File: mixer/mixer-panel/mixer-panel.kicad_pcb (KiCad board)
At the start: 2 copper layers, 40.3 x 128.5 mm, 14 parts

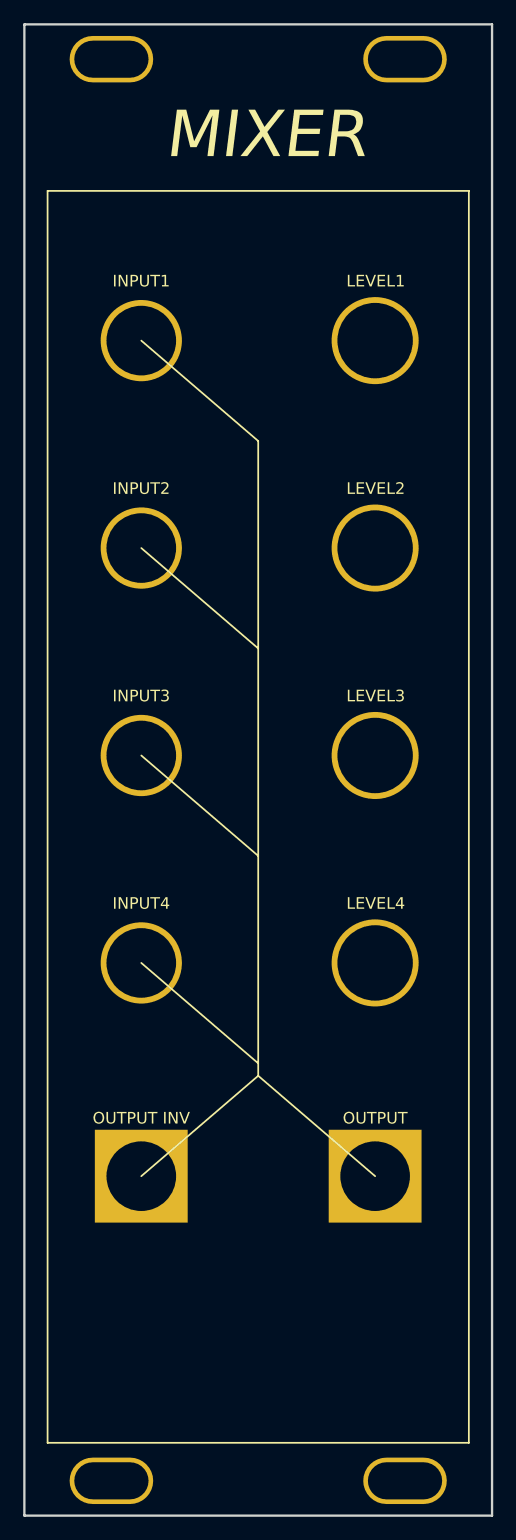
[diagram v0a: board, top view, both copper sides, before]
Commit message: Added rev2 of mixer. Fixed opamp configuation and panel connector layout
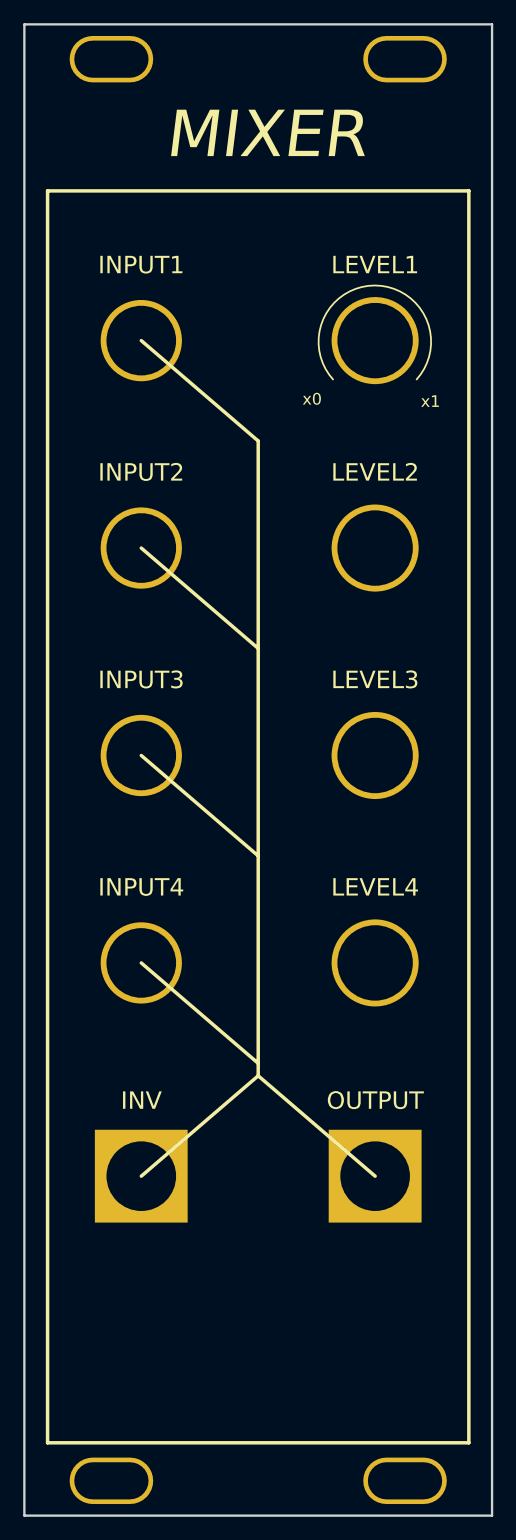
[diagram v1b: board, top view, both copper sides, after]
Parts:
- INV: renamed from OUTPUT INV
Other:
- board text added: "REV2"
- board text added: "x0"
- board text added: "x1"
- board text removed: "REV1"
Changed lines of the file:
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@@
   (footprint "Eurorack_Panel_Designs:3.5MM_Jack_Panel_Output_Plated" locked (layer "F.Cu")
     (at 147.225 132.75)
-    (fp_text reference "OUTPUT" (at 0 -5 unlocked) (layer "F.SilkS")
-      (effects (font (size 1 1) (thickness 0.15)))
+    (fp_text reference "OUTPUT" (at 0 -6.5 unlocked) (layer "F.SilkS")
+      (effects (font (size 1.5 1.5) (thickness 0.3)))
     )
     (fp_text value "3.5MM_Jack_Panel_Output_Plated" (at 0.826 -6.818 unlocked) (layer "F.Fab") hide
@@
     (at 147.225 78.625)
     (attr through_hole)
-    (fp_text reference "LEVEL2" (at 0.0508 -5.1308 unlocked) (layer "F.SilkS")
-      (effects (font (size 1 1) (thickness 0.15)))
+    (fp_text reference "LEVEL2" (at 0 -6.505 unlocked) (layer "F.SilkS")
+      (effects (font (size 1.5 1.5) (thickness 0.3)))
     )
     (fp_text value "Alpha_Plastic_Pot_Plated" (at 0 -5.4356 unlocked) (layer "F.Fab") hide
-      (effects (font (size 1 1) (thickness 0.15)))
-    )
-    (fp_text user "${REFERENCE}" (at 0 2.5 unlocked) (layer "F.Fab")
       (effects (font (size 1 1) (thickness 0.15)))
     )
@@
   (footprint "Eurorack_Panel_Designs:3.5MM_Jack_Panel_Output_Plated" (layer "F.Cu")
     (at 127.075 132.75)
-    (fp_text reference "OUTPUT INV" (at 0 -5 unlocked) (layer "F.SilkS")
-      (effects (font (size 1 1) (thickness 0.15)))
+    (fp_text reference "INV" (at 0 -6.5 unlocked) (layer "F.SilkS")
+      (effects (font (size 1.5 1.5) (thickness 0.3)))
     )
     (fp_text value "3.5MM_Jack_Panel_Output_Plated" (at 0.826 -6.818 unlocked) (layer "F.Fab") hide
@@
   (footprint "Eurorack_Panel_Designs:3.5MM_Jack_Panel_Input_Plated" (layer "F.Cu")
     (at 127.075 96.5)
-    (fp_text reference "INPUT3" (at 0 -5.1308 unlocked) (layer "F.SilkS")
-      (effects (font (size 1 1) (thickness 0.15)))
+    (fp_text reference "INPUT3" (at 0 -6.5 unlocked) (layer "F.SilkS")
+      (effects (font (size 1.5 1.5) (thickness 0.3)))
     )
     (fp_text value "3.5MM_Jack_Panel_Input_Plated" (at 0 -4.1896 unlocked) (layer "F.Fab") hide
@@
     (at 147.225 96.5)
     (attr through_hole)
-    (fp_text reference "LEVEL3" (at 0.0508 -5.1308 unlocked) (layer "F.SilkS")
-      (effects (font (size 1 1) (thickness 0.15)))
+    (fp_text reference "LEVEL3" (at 0 -6.5 unlocked) (layer "F.SilkS")
+      (effects (font (size 1.5 1.5) (thickness 0.3)))
     )
     (fp_text value "Alpha_Plastic_Pot_Plated" (at 0 -5.4356 unlocked) (layer "F.Fab") hide
@@
   (footprint "Eurorack_Panel_Designs:3.5MM_Jack_Panel_Input_Plated" (layer "F.Cu")
     (at 127.075 60.75)
-    (fp_text reference "INPUT1" (at 0 -5.1308 unlocked) (layer "F.SilkS")
-      (effects (font (size 1 1) (thickness 0.15)))
+    (fp_text reference "INPUT1" (at 0 -6.5 unlocked) (layer "F.SilkS")
+      (effects (font (size 1.5 1.5) (thickness 0.3)))
     )
     (fp_text value "3.5MM_Jack_Panel_Input_Plated" (at 0 -4.1896 unlocked) (layer "F.Fab") hide
@@
   (footprint "Eurorack_Panel_Designs:3.5MM_Jack_Panel_Input_Plated" (layer "F.Cu")
     (at 127.075 78.625)
-    (fp_text reference "INPUT2" (at 0 -5.1308 unlocked) (layer "F.SilkS")
-      (effects (font (size 1 1) (thickness 0.15)))
+    (fp_text reference "INPUT2" (at 0 -6.505 unlocked) (layer "F.SilkS")
+      (effects (font (size 1.5 1.5) (thickness 0.3)))
     )
     (fp_text value "3.5MM_Jack_Panel_Input_Plated" (at 0 -4.1896 unlocked) (layer "F.Fab") hide
@@
   (footprint "Eurorack_Panel_Designs:3.5MM_Jack_Panel_Input_Plated" (layer "F.Cu")
     (at 127.075 114.375)
-    (fp_text reference "INPUT4" (at 0 -5.1308 unlocked) (layer "F.SilkS")
-      (effects (font (size 1 1) (thickness 0.15)))
+    (fp_text reference "INPUT4" (at 0 -6.5 unlocked) (layer "F.SilkS")
+      (effects (font (size 1.5 1.5) (thickness 0.3)))
     )
     (fp_text value "3.5MM_Jack_Panel_Input_Plated" (at 0 -4.1896 unlocked) (layer "F.Fab") hide
@@
     (at 147.225 114.375)
     (attr through_hole)
-    (fp_text reference "LEVEL4" (at 0.0508 -5.1308 unlocked) (layer "F.SilkS")
-      (effects (font (size 1 1) (thickness 0.15)))
+    (fp_text reference "LEVEL4" (at 0 -6.5 unlocked) (layer "F.SilkS")
+      (effects (font (size 1.5 1.5) (thickness 0.3)))
     )
     (fp_text value "Alpha_Plastic_Pot_Plated" (at 0 -5.4356 unlocked) (layer "F.Fab") hide
@@
     (at 147.225 60.75)
     (attr through_hole)
-    (fp_text reference "LEVEL1" (at 0.0508 -5.1308 unlocked) (layer "F.SilkS")
-      (effects (font (size 1 1) (thickness 0.15)))
+    (fp_text reference "LEVEL1" (at 0 -6.5 unlocked) (layer "F.SilkS")
+      (effects (font (size 1.5 1.5) (thickness 0.3)))
     )
     (fp_text value "Alpha_Plastic_Pot_Plated" (at 0 -5.4356 unlocked) (layer "F.Fab") hide
-      (effects (font (size 1 1) (thickness 0.15)))
-    )
-    (fp_text user "${REFERENCE}" (at 0 2.5 unlocked) (layer "F.Fab")
       (effects (font (size 1 1) (thickness 0.15)))
     )
@@
     (pad "" thru_hole oval locked (at 0 0) (size 7.2 4) (drill oval 6.4 3.2) (layers *.Cu *.Mask))
   )
-  (gr_line (start 127.075 96.5) (end 137.15 105.15) (layer "F.SilkS") (width 0.15))
-  (gr_line (start 137.15 124.1) (end 147.225 132.75) (layer "F.SilkS") (width 0.15))
-  (gr_rect locked (start 119 47.85) (end 155.3 155.725) (layer "F.SilkS") (width 0.15) (fill none))
-  (gr_line (start 127.075 114.375) (end 137.15 123.025) (layer "F.SilkS") (width 0.15))
-  (gr_line (start 127.075 78.625) (end 137.15 87.275) (layer "F.SilkS") (width 0.15))
-  (gr_line (start 137.15 124.1) (end 127.075 132.75) (layer "F.SilkS") (width 0.15))
-  (gr_line (start 127.075 60.75) (end 137.15 69.4) (layer "F.SilkS") (width 0.15))
-  (gr_line (start 137.15 69.4) (end 137.15 124.1) (layer "F.SilkS") (width 0.15))
+  (gr_line (start 127.075 96.5) (end 137.15 105.15) (layer "F.SilkS") (width 0.3))
+  (gr_line (start 137.15 124.1) (end 147.225 132.75) (layer "F.SilkS") (width 0.3))
+  (gr_rect locked (start 119 47.85) (end 155.3 155.725) (layer "F.SilkS") (width 0.3) (fill none))
+  (gr_line (start 127.075 114.375) (end 137.15 123.025) (layer "F.SilkS") (width 0.3))
+  (gr_line (start 127.075 78.625) (end 137.15 87.275) (layer "F.SilkS") (width 0.3))
+  (gr_arc (start 143.6 64.098193) (mid 147.2 56) (end 150.8 64.098193) (layer "F.SilkS") (width 0.15))
+  (gr_line (start 137.15 124.1) (end 127.075 132.75) (layer "F.SilkS") (width 0.3))
+  (gr_line (start 127.075 60.75) (end 137.15 69.4) (layer "F.SilkS") (width 0.3))
+  (gr_line (start 137.15 69.4) (end 137.15 124.1) (layer "F.SilkS") (width 0.3))
   (gr_line (start 117 47.75) (end 157.3 47.75) (layer "Dwgs.User") (width 0.15))
   (gr_line (start 117 147.75) (end 157.3 147.75) (layer "Dwgs.User") (width 0.15))
   (gr_rect locked (start 117 33.5) (end 157.3 162) (layer "Edge.Cuts") (width 0.2) (fill none))
-  (gr_text "REV1" (at 137.1 158.7) (layer "B.SilkS")
+  (gr_text "REV2" (at 137.1 158.7) (layer "B.SilkS")
     (effects (font (size 1 1) (thickness 0.15)) (justify mirror))
   )
+  (gr_text "x0" (at 141.8 65.8) (layer "F.SilkS")
+    (effects (font (size 1 1) (thickness 0.15)))
+  )
+  (gr_text "x1" (at 152 66) (layer "F.SilkS")
+    (effects (font (size 1 1) (thickness 0.15)))
+  )
   (gr_text "MIXER" (at 137.8 43) (layer "F.SilkS")
-    (effects (font (size 4 4) (thickness 0.3) italic))
+    (effects (font (size 4 4) (thickness 0.35) italic))
   )
   (gr_text "PCB_BOTTOM" (at 122.4 149) (layer "Dwgs.User")

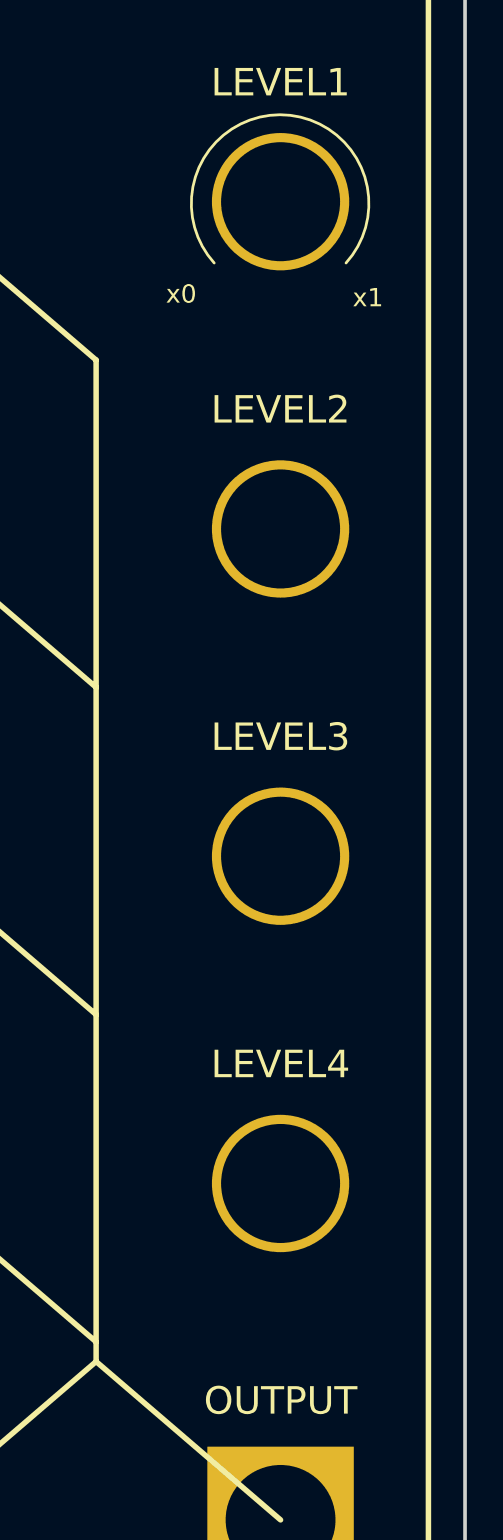
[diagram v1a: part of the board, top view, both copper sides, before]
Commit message: Updated graphics on rev2 mixer panel
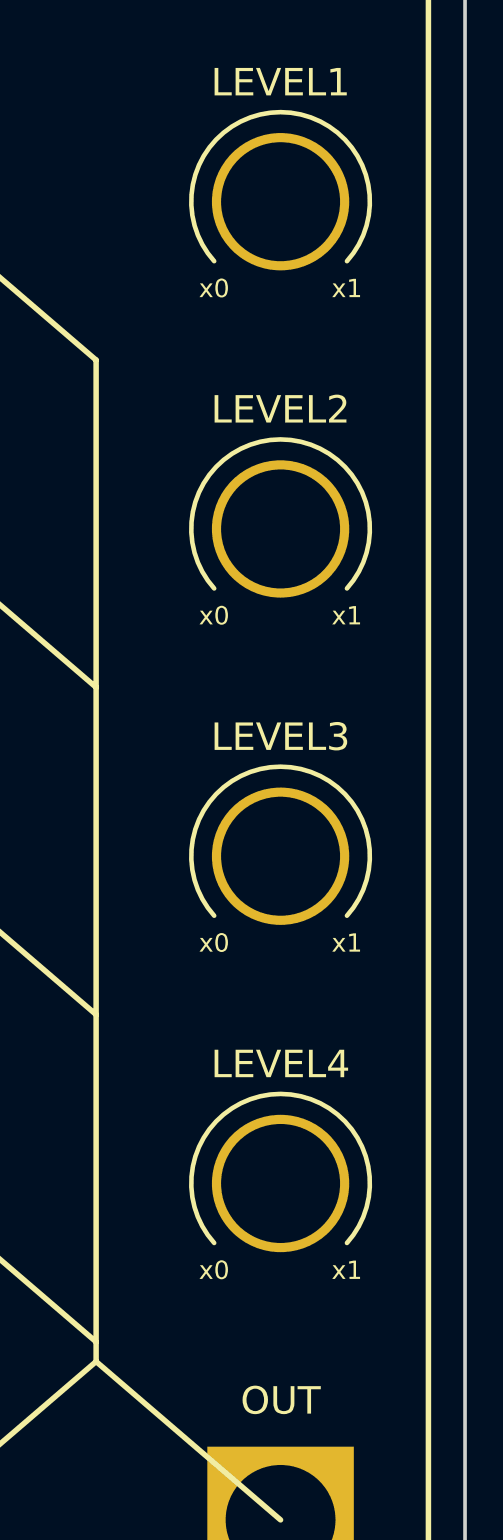
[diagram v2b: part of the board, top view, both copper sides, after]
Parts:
- renumbered OUTPUT to OUT
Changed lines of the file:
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@@
   (footprint "Eurorack_Panel_Designs:3.5MM_Jack_Panel_Output_Plated" locked (layer "F.Cu")
     (at 147.225 132.75)
-    (fp_text reference "OUTPUT" (at 0 -6.5 unlocked) (layer "F.SilkS")
+    (fp_text reference "OUT" (at 0 -6.5 unlocked) (layer "F.SilkS")
       (effects (font (size 1.5 1.5) (thickness 0.3)))
     )
@@
       (effects (font (size 1 1) (thickness 0.15)))
     )
-    (fp_text user "${REFERENCE}" (at 0 2.5 unlocked) (layer "F.Fab")
-      (effects (font (size 1 1) (thickness 0.15)))
-    )
     (pad "" thru_hole circle locked (at 0 0) (size 7.5 7.5) (drill 6.5) (layers *.Cu *.Mask))
   )
@@
     )
     (fp_text value "Alpha_Plastic_Pot_Plated" (at 0 -5.4356 unlocked) (layer "F.Fab") hide
-      (effects (font (size 1 1) (thickness 0.15)))
-    )
-    (fp_text user "${REFERENCE}" (at 0 2.5 unlocked) (layer "F.Fab")
       (effects (font (size 1 1) (thickness 0.15)))
     )
@@
   (gr_line (start 127.075 114.375) (end 137.15 123.025) (layer "F.SilkS") (width 0.3))
   (gr_line (start 127.075 78.625) (end 137.15 87.275) (layer "F.SilkS") (width 0.3))
-  (gr_arc (start 143.6 64.098193) (mid 147.2 56) (end 150.8 64.098193) (layer "F.SilkS") (width 0.15))
+  (gr_arc (start 143.6 117.625) (mid 147.225 109.483116) (end 150.85 117.625) (layer "F.SilkS") (width 0.25))
+  (gr_arc locked (start 143.6 81.875) (mid 147.225 73.733116) (end 150.85 81.875) (layer "F.SilkS") (width 0.25))
+  (gr_arc (start 143.6 99.75) (mid 147.225 91.608116) (end 150.85 99.75) (layer "F.SilkS") (width 0.25))
+  (gr_arc locked (start 143.6 64) (mid 147.225 55.858116) (end 150.85 64) (layer "F.SilkS") (width 0.25))
   (gr_line (start 137.15 124.1) (end 127.075 132.75) (layer "F.SilkS") (width 0.3))
   (gr_line (start 127.075 60.75) (end 137.15 69.4) (layer "F.SilkS") (width 0.3))
@@
     (effects (font (size 1 1) (thickness 0.15)) (justify mirror))
   )
-  (gr_text "x0" (at 141.8 65.8) (layer "F.SilkS")
-    (effects (font (size 1 1) (thickness 0.15)))
-  )
-  (gr_text "x1" (at 152 66) (layer "F.SilkS")
+  (gr_text "x0" (at 143.6 65.5) (layer "F.SilkS")
+    (effects (font (size 1 1) (thickness 0.15)))
+  )
+  (gr_text "x0" (at 143.6 101.25) (layer "F.SilkS")
+    (effects (font (size 1 1) (thickness 0.15)))
+  )
+  (gr_text "x1" (at 150.85 119.125) (layer "F.SilkS")
+    (effects (font (size 1 1) (thickness 0.15)))
+  )
+  (gr_text "x1" (at 150.85 65.5) (layer "F.SilkS")
+    (effects (font (size 1 1) (thickness 0.15)))
+  )
+  (gr_text "x1" (at 150.85 83.375) (layer "F.SilkS")
+    (effects (font (size 1 1) (thickness 0.15)))
+  )
+  (gr_text "x0" (at 143.6 83.375) (layer "F.SilkS")
     (effects (font (size 1 1) (thickness 0.15)))
   )
@@
     (effects (font (size 4 4) (thickness 0.35) italic))
   )
+  (gr_text "x0" (at 143.6 119.125) (layer "F.SilkS")
+    (effects (font (size 1 1) (thickness 0.15)))
+  )
+  (gr_text "x1" (at 150.85 101.25) (layer "F.SilkS")
+    (effects (font (size 1 1) (thickness 0.15)))
+  )
   (gr_text "PCB_BOTTOM" (at 122.4 149) (layer "Dwgs.User")
